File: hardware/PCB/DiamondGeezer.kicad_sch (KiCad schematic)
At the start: 32 parts, among them J1 ANCHORPIN, J10 ANCHORPIN, J11 ANCHORPIN, J12 ANCHORPIN, J13 ANCHORPIN, J2 OLED Screen Interface, J3 ANCHORPIN, J6 ANCHORPIN, J7 ANCHORPIN, J8 ANCHORPIN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

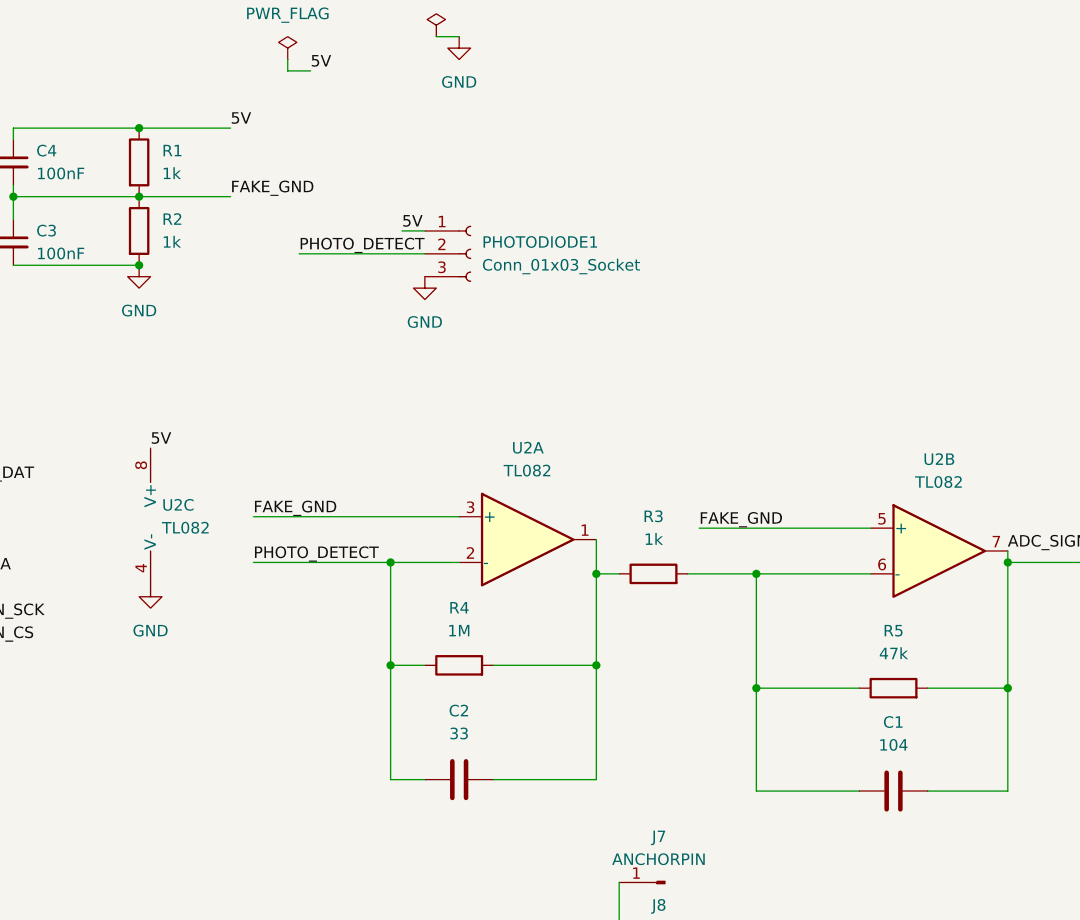
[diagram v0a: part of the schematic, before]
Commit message: Updated values for R1, R2, R4, R5, C1, C2, C3, C4 based on new experiments
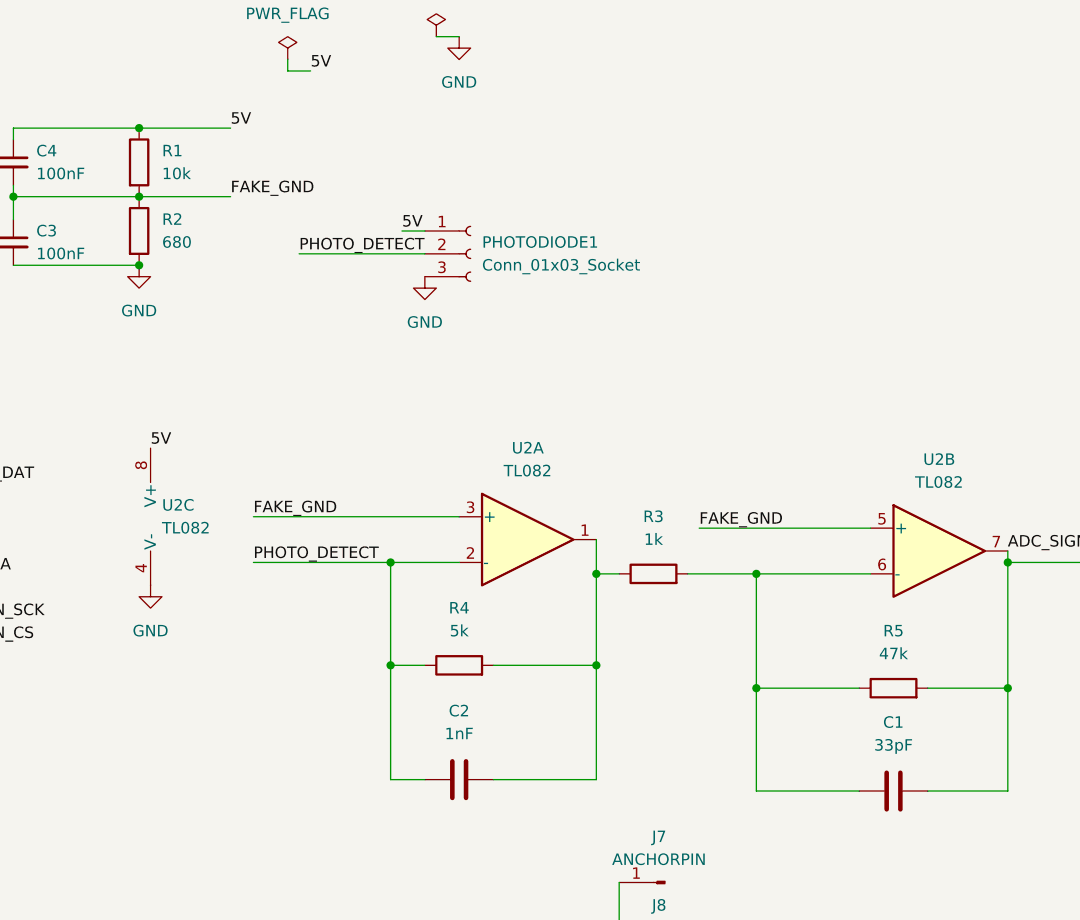
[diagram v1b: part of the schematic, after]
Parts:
- C1: value 104 -> 33pF
- C2: value 33 -> 1nF
- R1: value 1k -> 10k
- R2: value 1k -> 680
- R4: value 1M -> 5k
